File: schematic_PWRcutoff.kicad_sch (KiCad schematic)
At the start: 29 parts, among them J1 Conn_01x02, J10 Conn_01x02, J11 Conn_01x02, J12 Conn_01x08, J13 Conn_01x08, J14 Conn_01x02, J15 Conn_01x02, J2 Conn_01x02, J3 Conn_01x02, J4 Conn_01x04, J5 Conn_01x02, J6 Conn_01x04, J7 Conn_01x02, J8 Conn_01x02, J9 Conn_01x02

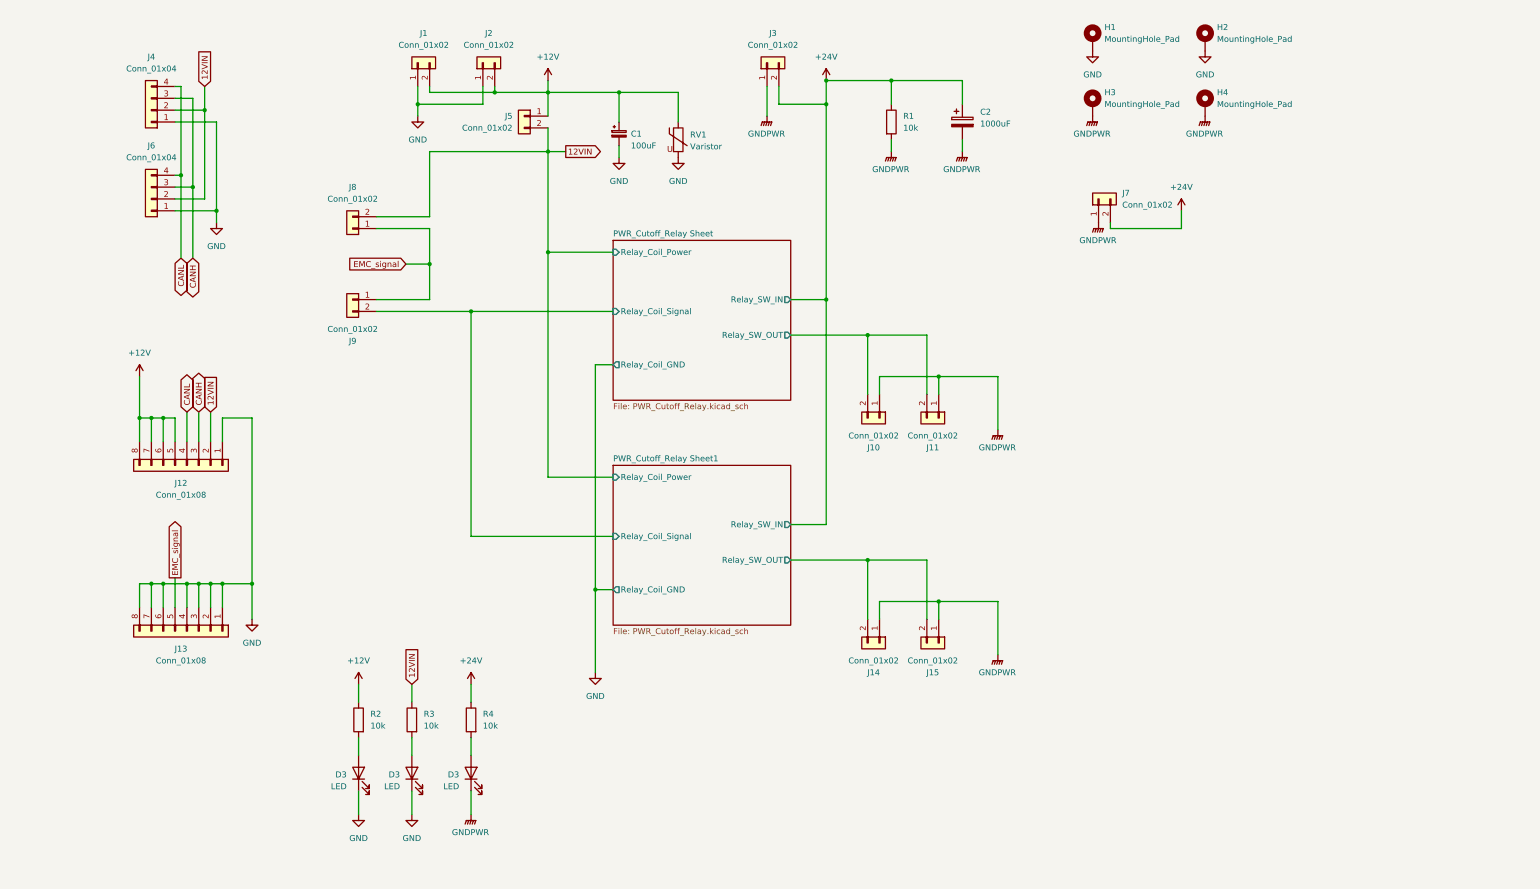
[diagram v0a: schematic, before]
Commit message: add STM32F103
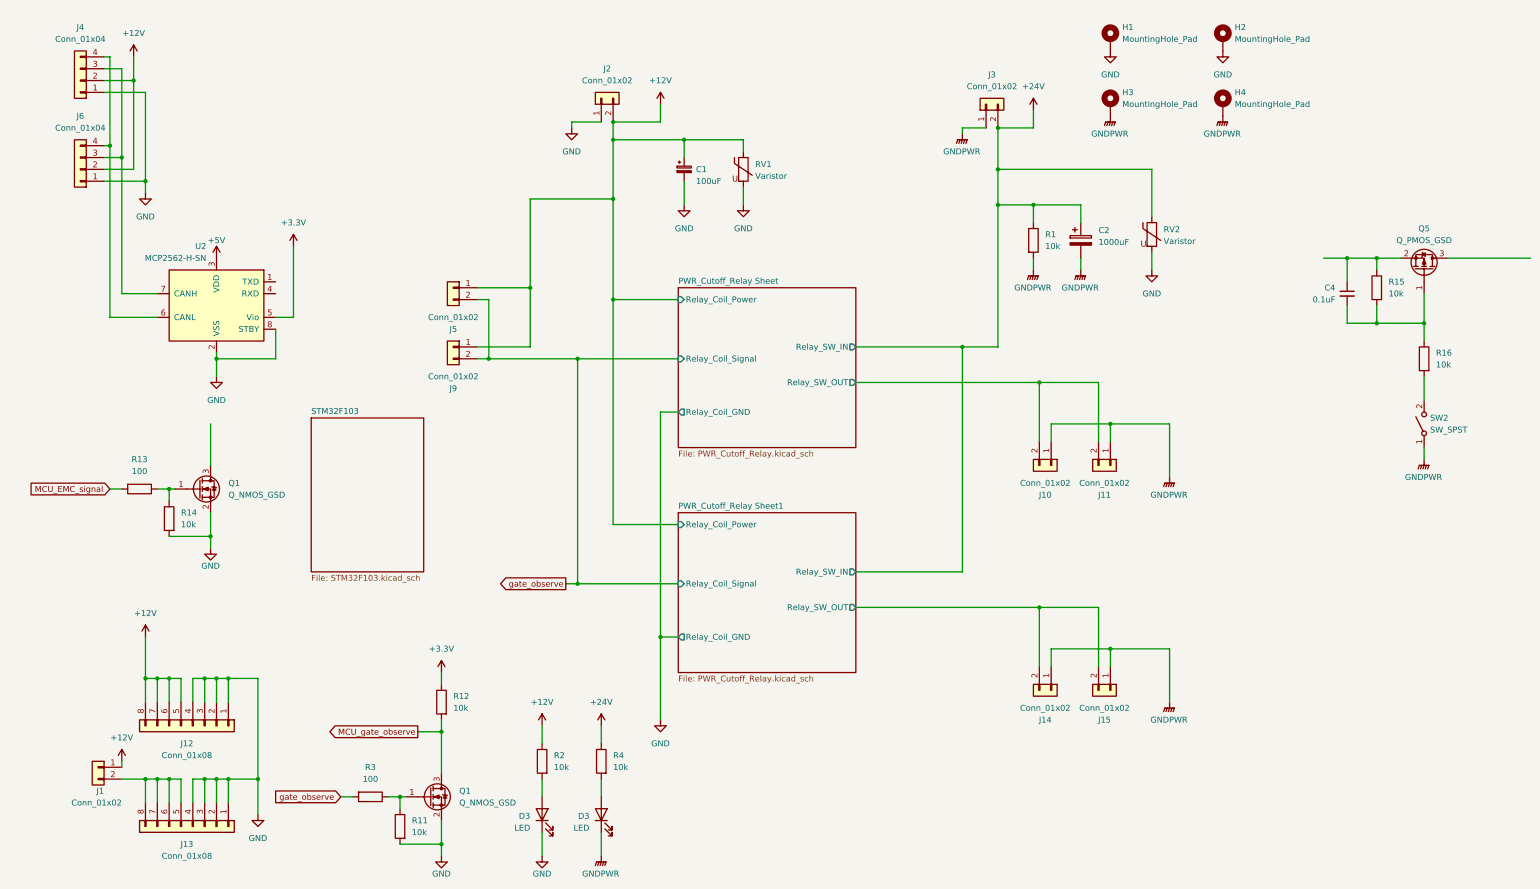
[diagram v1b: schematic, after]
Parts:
- removed D3: LED, LED_SMD:LED_0603_1608Metric_Pad1.05x0.95mm_HandSolder, symbol Device:LED
- removed J7, J8: Conn_01x02, Connector_PinHeader_2.54mm:PinHeader_1x02_P2.54mm_Vertical, symbol Connector_Generic:Conn_01x02
- added C4: 0.1uF, Capacitor_SMD:C_0603_1608Metric_Pad1.08x0.95mm_HandSolder, symbol Device:C_Small
- added Q1 (x2): Q_NMOS_GSD, Package_TO_SOT_SMD:SOT-23, symbol Device:Q_NMOS_GSD
- added Q5: Q_PMOS_GSD, Package_TO_SOT_THT:TO-3P-3_Vertical, symbol Device:Q_PMOS_GSD
- added R11, R12, R14, R15, R16: 10k, Resistor_SMD:R_0603_1608Metric_Pad0.98x0.95mm_HandSolder, symbol Device:R
- added R13: 100, Resistor_SMD:R_0603_1608Metric_Pad0.98x0.95mm_HandSolder, symbol Device:R
- added RV2: Varistor, Varistor:RV_Disc_D12mm_W4.5mm_P7.5mm, symbol Device:Varistor
- added SW2: SW_SPST, symbol Switch:SW_SPST
- added U2: MCP2562-H-SN, Package_SO:SOIC-8_3.9x4.9mm_P1.27mm, symbol Interface_CAN_LIN:MCP2562-H-SN
- J1: footprint Connector_AMASS:AMASS_XT60-F_1x02_P7.20mm_Vertical -> Connector_PinHeader_2.54mm:PinHeader_1x02_P2.54mm_Vertical
- J5: footprint Connector_PinHeader_2.54mm:PinHeader_1x02_P2.54mm_Vertical -> Connector_JST:JST_XA_B02B-XASK-1_1x02_P2.50mm_Vertical
- R3: value 10k -> 100
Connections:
- net PWR_Cutoff_Relay Sheet/Relay_Coil_Signal is gone; now on net gate_observe: J9.2 (Pin_2)
- net +12V: now also J1.1 (Pin_1), J4.2 (Pin_2), J6.2 (Pin_2), J9.1 (Pin_1); no longer J1.2 (Pin_2)
- net +24V: now also RV2.1
- net GND: now also J12.2 (Pin_2), J12.3 (Pin_3), J12.4 (Pin_4), Q1.2 (S), Q1.2 (S), R11.2, R14.2, RV2.2, U2.2 (VSS), U2.8 (STBY); no longer J1.1 (Pin_1), J13.6 (Pin_6), J13.7 (Pin_7), J13.8 (Pin_8)
- net GNDPWR: now also SW2.1 (A)
- net gate_observe: now reaches R3.2
- net gate_observe: now also J5.2 (Pin_2)
- removed net 12VIN: J12.2 (Pin_2), J4.2 (Pin_2), J5.2 (Pin_2), J6.2 (Pin_2), R3.1
- net CANH: no longer names the net of J4.3 (Pin_3), J6.3 (Pin_3)
- net CANH: now also U2.7 (CANH); no longer J12.3 (Pin_3)
- net CANL: no longer names the net of J4.4 (Pin_4), J6.4 (Pin_4)
- net CANL: now also U2.6 (CANL); no longer J12.4 (Pin_4)
- net EMC_signal: no longer names the net of J13.5 (Pin_5)
- net EMC_signal: now also J1.2 (Pin_2), J13.6 (Pin_6), J13.7 (Pin_7), J13.8 (Pin_8); no longer J9.1 (Pin_1)
- new net: Q1.1 (G), R13.1, R14.1
- new net: R16.2, SW2.2 (B)
- new net: C4.1, Q5.2 (S), R15.1
- new net: C4.2, Q5.1 (G), R15.2, R16.1
- new net: Q1.1 (G), R11.1, R3.1
- new net +3.3V: R12.1, U2.5 (Vio)
- new net +5V: U2.3 (VDD)
- new net MCU_EMC_signal: R13.2
- new net MCU_gate_observe: Q1.3 (D), R12.2
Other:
- added sheet STM32F103 (STM32F103.kicad_sch)
- moved on the sheet: C1, C2, D3, H1, H2, H3, H4, J10, J11, J12, J13, J14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

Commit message: add switch, EMS & MCU
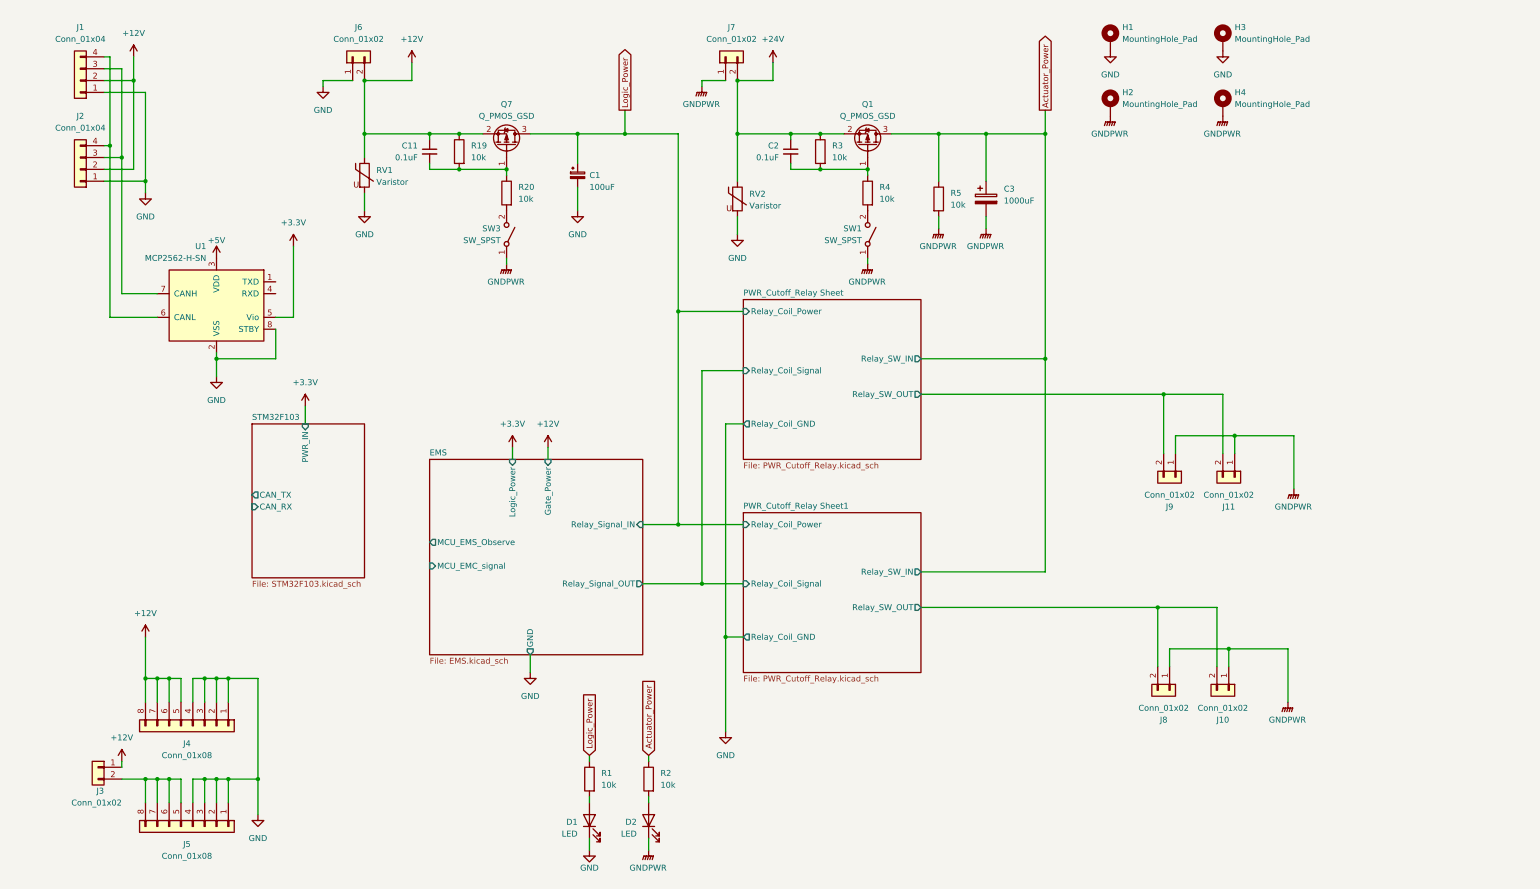
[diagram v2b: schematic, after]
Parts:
- removed J3: Conn_01x02, RDC_general:XT90-M, symbol Connector_Generic:Conn_01x02
- removed J5, J9: Conn_01x02, Connector_JST:JST_XA_B02B-XASK-1_1x02_P2.50mm_Vertical, symbol Connector_Generic:Conn_01x02
- removed Q1 (x2): Q_NMOS_GSD, Package_TO_SOT_SMD:SOT-23, symbol Device:Q_NMOS_GSD
- removed R11, R12, R14: 10k, Resistor_SMD:R_0603_1608Metric_Pad0.98x0.95mm_HandSolder, symbol Device:R
- removed R13, R3: 100, Resistor_SMD:R_0603_1608Metric_Pad0.98x0.95mm_HandSolder, symbol Device:R
- added C11: 0.1uF, Capacitor_SMD:C_0603_1608Metric_Pad1.08x0.95mm_HandSolder, symbol Device:C_Small
- added J7: Conn_01x02, RDC_general:XT90-M, symbol Connector_Generic:Conn_01x02
- added Q7: Q_PMOS_GSD, Package_TO_SOT_THT:TO-3P-3_Vertical, symbol Device:Q_PMOS_GSD
- added R19, R20: 10k, Resistor_SMD:R_0603_1608Metric_Pad0.98x0.95mm_HandSolder, symbol Device:R
- added SW3: SW_SPST, symbol Switch:SW_SPST
- renumbered C4 to C2, C2 to C3, D3 to D1, D3 to D2, H3 to H2, H2 to H3, J4 to J1, J15 to J10, J6 to J2, J1 to J3, J12 to J4, J13 to J5, J2 to J6, J14 to J8, J10 to J9, Q5 to Q1, R2 to R1, R4 to R2, R15 to R3, R16 to R4, R1 to R5, SW2 to SW1, U2 to U1
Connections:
- net +12V: now also C11.1, Q7.2 (S), R19.1; no longer C1.1, R1.1
- net +24V: now also C2.1, Q1.2 (S), R3.1, J7.2 (Pin_2); no longer C3.1, R2.1, R5.1
- net GNDPWR: now also J7.1 (Pin_1), SW3.1 (A)
- net Actuator_Power: now reaches Q1.3 (D)
- net Actuator_Power: now also C3.1, R2.1, R5.1
- new net: C11.2, Q7.1 (G), R19.2, R20.1
- new net: R20.2, SW3.2 (B)
- new net Logic_Power: C1.1, Q7.3 (D), R1.1
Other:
- added sheet EMS (EMS.kicad_sch)
- sheet STM32F103 ports: added CAN_RX, CAN_TX, PWR_IN; removed none
- moved on the sheet: C2, C3, D1, D2, J10, J11, J6, J8, J9, Q1, R1, R2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

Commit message: precompreate design
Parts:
- removed C1: 100uF, Capacitor_THT:CP_Radial_D8.0mm_P5.00mm, symbol Device:C_Polarized_Small
- removed J3: Conn_01x02, Connector_PinHeader_2.54mm:PinHeader_1x02_P2.54mm_Vertical, symbol Connector_Generic:Conn_01x02
- removed J4, J5: Conn_01x08, Connector_PinHeader_2.54mm:PinHeader_1x08_P2.54mm_Vertical, symbol Connector_Generic:Conn_01x08
- removed J6: Conn_01x02, Connector_AMASS:AMASS_XT60-M_1x02_P7.20mm_Vertical, symbol Connector_Generic:Conn_01x02
- removed Q1: Q_PMOS_GSD, Package_TO_SOT_THT:TO-3P-3_Vertical, symbol Device:Q_PMOS_GSD
- removed RV2: Varistor, Varistor:RV_Disc_D12mm_W4.5mm_P7.5mm, symbol Device:Varistor
- added C1: 1000uF, Capacitor_THT:CP_Radial_D16.0mm_P7.50mm, symbol Device:C_Polarized
- added C12, C15: 0.1uF, Capacitor_SMD:C_0603_1608Metric_Pad1.08x0.95mm_HandSolder, symbol Device:C_Small
- added D7: LED, LED_SMD:LED_0603_1608Metric_Pad1.05x0.95mm_HandSolder, symbol Device:LED
- added J14: STlink_v3, RDC_general:JTAG_box_connector, symbol Connector_Generic:Conn_02x07_Odd_Even
- added JP1: Jumper, Connector_PinHeader_2.54mm:PinHeader_1x02_P2.54mm_Vertical, symbol Jumper:Jumper_2_Open
- added Q1, Q8, Q9: Q_PMOS_GSD, Package_TO_SOT_SMD:TO-252-2, symbol Device:Q_PMOS_GDS
- added R21: 120, Resistor_SMD:R_0603_1608Metric_Pad0.98x0.95mm_HandSolder, symbol Device:R
- added R23, R27, R28, R29, R30, R31: 10k, Resistor_SMD:R_0603_1608Metric_Pad0.98x0.95mm_HandSolder, symbol Device:R
- added SW2: SW_DIP_x04, Button_Switch_SMD:SW_DIP_SPSTx04_Slide_Copal_CHS-04B_W7.62mm_P1.27mm, symbol Switch:SW_DIP_x04
- C3: footprint Capacitor_THT:CP_Radial_D18.0mm_P7.50mm -> Capacitor_THT:CP_Radial_D16.0mm_P7.50mm
- Q7: footprint Package_TO_SOT_THT:TO-3P-3_Vertical -> Package_TO_SOT_SMD:TO-252-2; symbol Device:Q_PMOS_GSD -> Device:Q_PMOS_GDS
- RV1: footprint Varistor:RV_Disc_D12mm_W4.5mm_P7.5mm -> Varistor:RV_Disc_D9mm_W4.5mm_P5mm
- SW1, SW3: footprint (none) -> RDC_general:Toggle_switch
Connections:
- net GNDPWR is gone; now on net GND: C3.2, D2.1 (K), H2.1, H4.1, J10.1 (Pin_1), J11.1 (Pin_1), J7.1 (Pin_1), J8.1 (Pin_1), J9.1 (Pin_1), R5.2, SW1.1 (A), SW3.1 (A)
- net +12V: no longer C11.1, Q7.2 (S), R19.1, RV1.1
- net +24V: now also C11.1, Q7.3 (S), R19.1, RV1.1, Q1.3 (S)
- net +3.3V: now also C15.2, J14.3 (Pin_3), SW2.5, SW2.6, SW2.7, SW2.8
- net +5V: now also C12.2
- net Actuator_Power: now also Q8.3 (S)
- net GND: now also C1.2, C12.1, C15.1, D7.1 (K), J14.5 (Pin_5), J14.7 (Pin_7), R27.2, R28.2, R29.2, R30.2, R31.2
- net STM32F103/CAN_RX: now also U1.4 (RXD)
- net STM32F103/CAN_TX: now also U1.1 (TXD)
- net at J1.4 (Pin_4), J2.4 (Pin_4), U1.6 (CANL): now also R21.2
- net at J1.3 (Pin_3), J2.3 (Pin_3), U1.7 (CANH): now also JP1.2 (B)
- net at C11.2, Q7.1 (G), R19.2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: now also Q9.1 (G)
- net at C2.2, R3.2, R4.1: now also Q1.1 (G), Q8.1 (G)
- net Logic_Power renamed Logic_line_Power
- net Logic_line_Power: now also C1.1, Q9.3 (S), R27.1; no longer Q7.3 (D)
- new net: Q7.2 (D), Q9.2 (D)
- new net: D7.2 (A), R23.2
- new net: Q1.2 (D), Q8.2 (D)
- new net: JP1.1 (A), R21.1
- new net MCU_running: R23.1
- new net STM32F103/CAN_ID1: R28.1, SW2.1
- new net STM32F103/CAN_ID2: R29.1, SW2.2
- new net STM32F103/CAN_ID3: R30.1, SW2.3
- new net STM32F103/CAN_ID4: R31.1, SW2.4
- new net STM32F103/SWCLK: J14.6 (Pin_6)
- new net STM32F103/SWDIO: J14.4 (Pin_4)
- new net STM32F103/SWO: J14.8 (Pin_8)
- no-connect marks 0 -> 8
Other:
- added sheet Logic_Power (Logic_Power.kicad_sch)
- sheet STM32F103 ports: added CAN_ID1, CAN_ID2, CAN_ID3, CAN_ID4, EMS_Observe, EMS_Signal, MCU_run, SWCLK, SWDIO, SWO; removed none
- moved on the sheet: C11, C2, C3, D1, D2, J1, J2, J7, Q7, R1, R19, R2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
